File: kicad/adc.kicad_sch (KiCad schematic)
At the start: 0 parts

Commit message: modified notes
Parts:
- added C23, C26, C28, C29, C30: 10u, symbol Device:C
- added C24, C25, C27, C31, C32, C37: 100n, symbol Device:C
- added C33, C35, C38: 150p, symbol Device:C
- added C34, C36: 1n, symbol Device:C
- added D8: ~, symbol CMF3216F-900-2P-T:D_TVS
- added J3: DOSIN-801-0031, symbol Connector:Conn_Coaxial
- added R21: 0R, symbol Device:R
- added R22: 49R9, symbol Device:R
- added R23, R25: 2M2, symbol Device:R
- added R24, R29, R30: 1k, symbol Device:R
- added R26: 6k8, symbol Device:R
- added R27: 22k, symbol Device:R
- added R28: 12k, symbol Device:R
- added U6: ADC141S626CIMM_NOPB, symbol Analog_ADC:ADC141S626
- added U7: REF3033AIDBZT, Package_TO_SOT_SMD:SOT-23, symbol Reference_Voltage:REF3033
- added U8, U9: MCP6001T-E/OT, Package_TO_SOT_SMD:SOT-23-5, symbol Amplifier_Operational:MCP6001-OT
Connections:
- new net: C34.1, R26.2, R27.1
- new net: C30.1, R22.2, U7.1 (IN)
- new net: C27.1, C28.1, U6.1 (VREF), U7.2 (OUT)
- new net: R21.1, U6.8 (SCLK)
- new net: C36.1, R27.2, R28.1
- new net +3.3VA: C25.1, C26.1, C31.2, C37.2, U6.10 (VA), U8.5 (V+), U9.5 (V+)
- new net +3V3: C23.1, C24.1, U6.9 (VIO)
- new net +5V: C29.1, R22.1
- new net ADC_IN+: C38.1, R29.2, U6.2 (+IN)
- new net ADC_IN-: C38.2, R30.2, U6.3 (-IN)
- new net GND: C23.2, C24.2, C25.2, C26.2, C27.2, C28.2, C29.2, C30.2, C31.1, C33.2, C34.2, C35.2, C37.1, D8.1 (A1), J3.2 (Ext), R25.1, U6.4 (GND), U6.5 (GND), U7.3 (GND), U8.2 (V-), U9.2 (V-)
- new net IN: D8.2 (A2), J3.1 (In), R24.1
- new net IN_AA_BUF_IN: C35.1, R28.2, U9.3 (+)
- new net IN_BUF: C32.2, R23.2, U8.3 (+)
- new net IN_BUF_OUT: R26.1, U8.1, U8.4 (-)
- new net IN_RF: C32.1, C33.1, R24.2, R25.2
- new net OUT_AA_BUF_IN: C36.2, R29.1, U9.1, U9.4 (-)
- new net SPI1_MISO: U6.7 (DOUT)
- new net SPI1_NSS: U6.6 (NCS)
- new net SPI1_SCK: R21.2
- new net VCOM: R23.1, R30.1
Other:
- note added: "14-Bit S/H ADC"
- note added: "3rd order Butterworth anti-aliasing (low-pass) filter fc=25kHz"
- note added: "Analog Front-End"
- note added: "BNC Connector"
- note added: "HP filter: fc=1.4Hz"
- note added: "Input voltage must be in +/- 1.65V range!"
- note added: "MCP6001: I/O Rail-to-Rail, Single-Supply (1V8 to 5V), high-impedance input CMOS, low bias currents, unity gain stable"
- note added: "PESD3V3L1BA,115"
- note added: "Rin=1.1M RF filter: fc=1.1MHz"
- note added: "Single-ended to 'balanced' conversion Both ADC inputs should be at same VCOM"
- note added: "Vref=3V3 Vref filter: fc=319Hz P(R, max)=0.1W -> I(R, max)=45mA"
- note added: "[3] ADC & Analog Front-End"

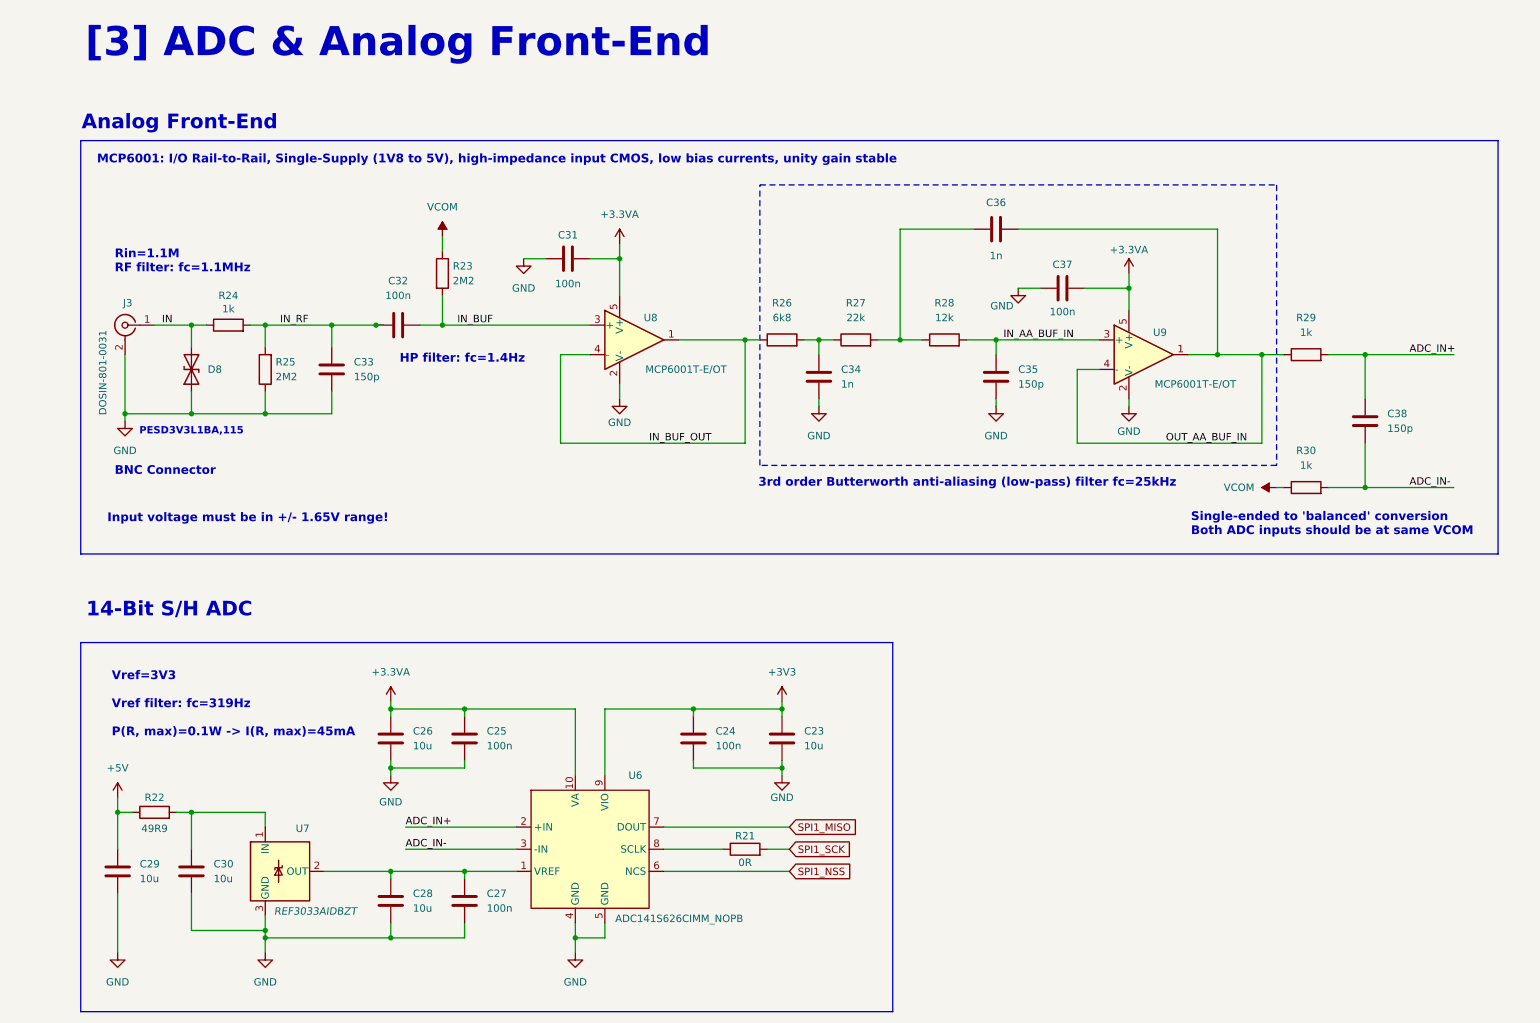
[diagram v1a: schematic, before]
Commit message: Updated parts numbering and notes
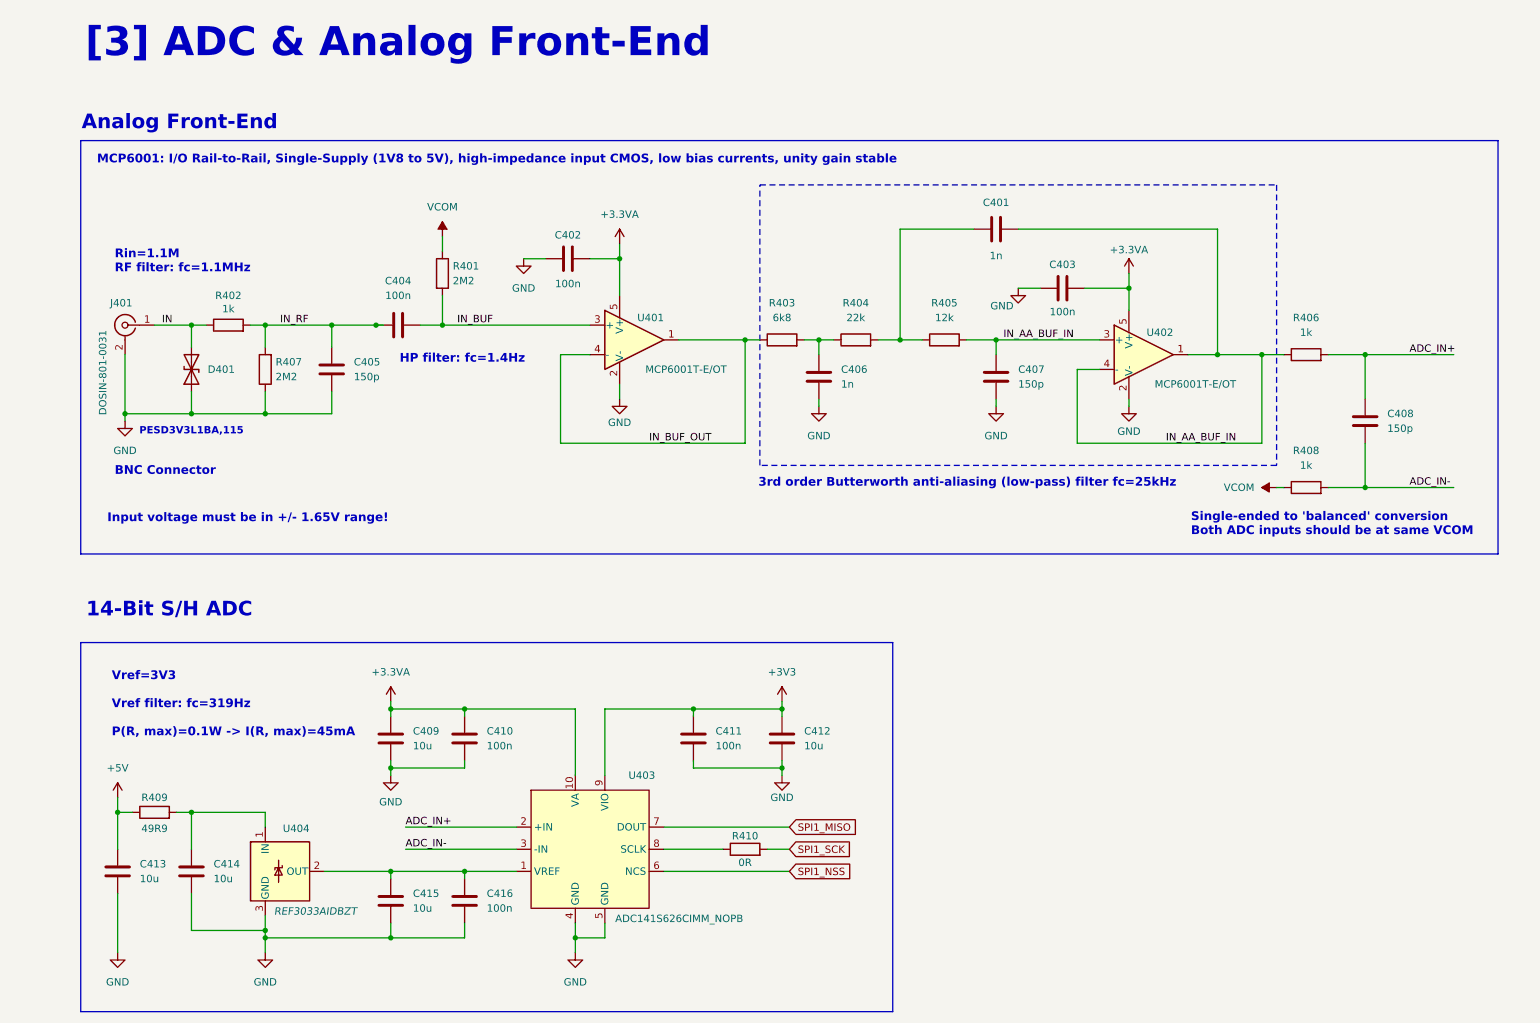
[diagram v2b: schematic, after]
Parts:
- renumbered C36 to C401, C31 to C402, C37 to C403, C32 to C404, C33 to C405, C34 to C406, C35 to C407, C38 to C408, C26 to C409, C25 to C410, C24 to C411, C23 to C412, C29 to C413, C30 to C414, C28 to C415, C27 to C416, D8 to D401, J3 to J401, R23 to R401, R24 to R402, R26 to R403, R27 to R404, R28 to R405, R29 to R406, R25 to R407, R30 to R408, R22 to R409, R21 to R410, U8 to U401, U9 to U402, U6 to U403, U7 to U404
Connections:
- net OUT_AA_BUF_IN is gone; now on net IN_AA_BUF_IN: C401.2, R406.1, U402.1, U402.4 (-)

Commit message: Save Progress
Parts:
- C401, C402, C403, C404, C405, C406, C407, C408, C410, C411, C416: footprint (none) -> Capacitor_SMD:C_0402_1005Metric
- C409, C412, C413, C414, C415: footprint (none) -> Capacitor_SMD:C_0603_1608Metric
- D401: value ~ -> D_TVS; footprint (none) -> Diode_SMD:D_SOD-323
- R401, R402, R403, R404, R405, R406, R407, R408, R409, R410: footprint (none) -> Resistor_SMD:R_0402_1005Metric
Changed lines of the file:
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@@
 			)
 		)
-		(property "Footprint" ""
+		(property "Footprint" "Resistor_SMD:R_0402_1005Metric"
 			(at 146.05 74.168 90)
 			(effects
@@
 			)
 		)
-		(property "Footprint" ""
+		(property "Footprint" "Capacitor_SMD:C_0402_1005Metric"
 			(at 113.03 57.4548 0)
 			(effects
@@
 			)
 		)
-		(property "Footprint" ""
+		(property "Footprint" "Capacitor_SMD:C_0402_1005Metric"
 			(at 69.5452 81.28 0)
 			(effects
@@
 			)
 		)
-		(property "Footprint" ""
+		(property "Footprint" "Resistor_SMD:R_0402_1005Metric"
 			(at 50.8 71.628 90)
 			(effects
@@
 			)
 		)
-		(property "Footprint" ""
+		(property "Footprint" "Capacitor_SMD:C_0402_1005Metric"
 			(at 198.12 62.5348 0)
 			(effects
@@
 			)
 		)
-		(property "Footprint" ""
+		(property "Footprint" "Capacitor_SMD:C_0603_1608Metric"
 			(at 79.7052 172.72 0)
 			(effects
@@
 			)
 		)
-		(property "Footprint" ""
+		(property "Footprint" "Capacitor_SMD:C_0603_1608Metric"
 			(at 79.7052 144.78 0)
 			(effects
@@
 			)
 		)
-		(property "Footprint" ""
+		(property "Footprint" "Capacitor_SMD:C_0402_1005Metric"
 			(at 83.82 68.8848 0)
 			(effects
@@
 			)
 		)
-		(property "Footprint" ""
+		(property "Footprint" "Resistor_SMD:R_0402_1005Metric"
 			(at 236.22 99.568 90)
 			(effects
@@
 			)
 		)
-		(property "Footprint" ""
+		(property "Footprint" "Capacitor_SMD:C_0402_1005Metric"
 			(at 153.3652 82.55 0)
 			(effects
@@
 			)
 		)
-		(property "Footprint" ""
+		(property "Footprint" "Resistor_SMD:R_0402_1005Metric"
 			(at 139.7 161.798 90)
 			(effects
@@
 			)
 		)
-		(property "Footprint" ""
+		(property "Footprint" "Capacitor_SMD:C_0603_1608Metric"
 			(at 147.0152 144.78 0)
 			(effects
@@
 			)
 		)
-		(property "Footprint" ""
+		(property "Footprint" "Capacitor_SMD:C_0402_1005Metric"
 			(at 92.4052 172.72 0)
 			(effects
@@
 			)
 		)
-		(property "Footprint" ""
+		(property "Footprint" "Resistor_SMD:R_0402_1005Metric"
 			(at 38.1 155.448 90)
 			(effects
@@
 			)
 		)
-		(property "Footprint" ""
+		(property "Footprint" "Capacitor_SMD:C_0603_1608Metric"
 			(at 32.7152 167.64 0)
 			(effects
@@
 			)
 		)
-		(property "Footprint" ""
+		(property "Footprint" "Capacitor_SMD:C_0402_1005Metric"
 			(at 247.3452 90.17 0)
 			(effects
@@
 			)
 		)
-		(property "Footprint" ""
+		(property "Footprint" "Resistor_SMD:R_0402_1005Metric"
 			(at 236.22 76.708 90)
 			(effects
@@
 			)
 		)
-		(property "Footprint" ""
+		(property "Footprint" "Capacitor_SMD:C_0402_1005Metric"
 			(at 186.69 52.3748 0)
 			(effects
@@
 			)
 		)
-		(property "Footprint" ""
+		(property "Footprint" "Resistor_SMD:R_0402_1005Metric"
 			(at 58.928 77.47 90)
 			(effects
@@
 			)
 		)
-		(property "Footprint" ""
+		(property "Footprint" "Capacitor_SMD:C_0603_1608Metric"
 			(at 45.4152 167.64 0)
 			(effects
@@
 			)
 		)
-		(property "Footprint" ""
+		(property "Footprint" "Resistor_SMD:R_0402_1005Metric"
 			(at 85.852 60.96 90)
 			(effects
@@
 			)
 		)
-		(property "Footprint" ""
+		(property "Footprint" "Resistor_SMD:R_0402_1005Metric"
 			(at 158.75 74.168 90)
 			(effects
@@
 			)
 		)
-		(property "Footprint" ""
+		(property "Footprint" "Resistor_SMD:R_0402_1005Metric"
 			(at 173.99 74.168 90)
 			(effects
@@
 		(dnp no)
 		(property "Reference" "D401"
-			(at 47.244 77.47 90)
+			(at 46.736 76.2 90)
 			(effects
 				(font
@@
 			)
 		)
-		(property "Value" "~"
-			(at 46.99 78.74 90)
+		(property "Value" "D_TVS"
+			(at 46.736 78.74 90)
 			(effects
 				(font
@@
 			)
 		)
-		(property "Footprint" ""
+		(property "Footprint" "Diode_SMD:D_SOD-323"
 			(at 44.45 77.47 0)
 			(effects
@@
 			)
 		)
-		(property "Footprint" ""
+		(property "Footprint" "Capacitor_SMD:C_0402_1005Metric"
 			(at 131.7752 144.78 0)
 			(effects
@@
 			)
 		)
-		(property "Footprint" ""
+		(property "Footprint" "Capacitor_SMD:C_0402_1005Metric"
 			(at 92.4052 144.78 0)
 			(effects
@@
 			)
 		)
-		(property "Footprint" ""
+		(property "Footprint" "Capacitor_SMD:C_0402_1005Metric"
 			(at 183.8452 82.55 0)
 			(effects
